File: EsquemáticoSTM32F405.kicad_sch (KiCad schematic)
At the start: 24 parts, among them SW3 XDTD-0304-215, U13 Green LED, U4 STM32F405RGT6, X1 32.768kHz 7pF SMD, X2 8Mhz 10pF

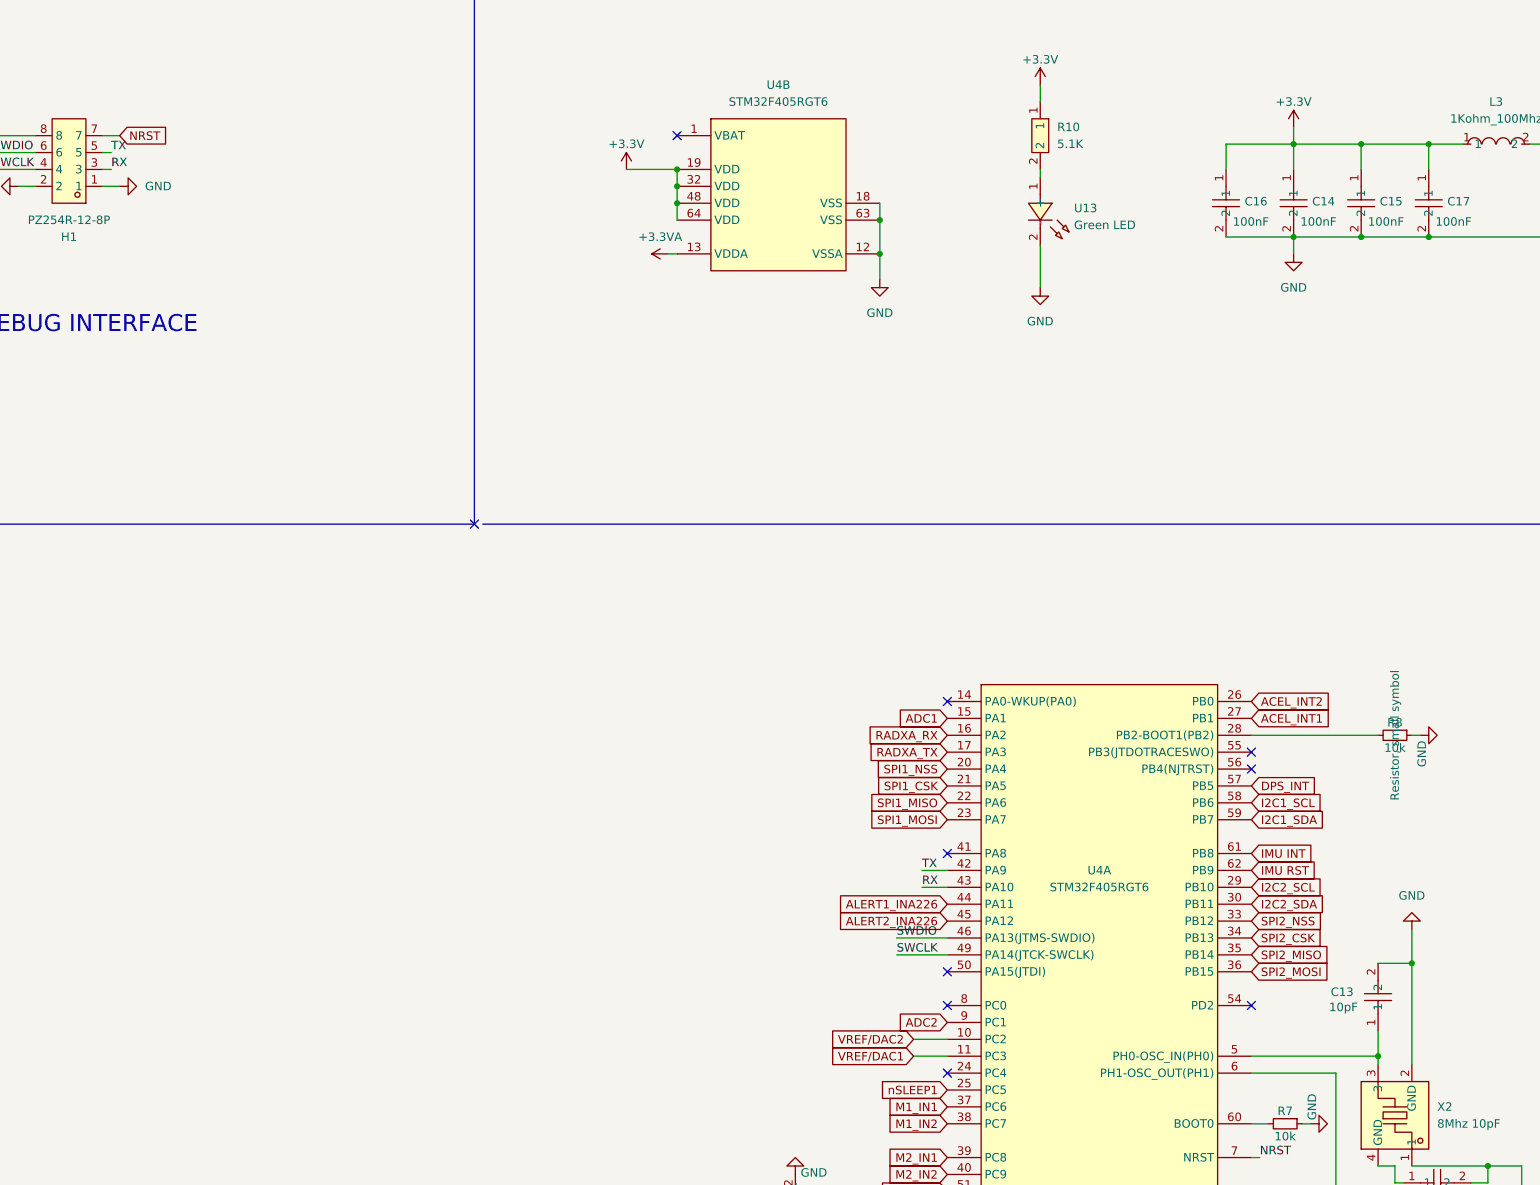
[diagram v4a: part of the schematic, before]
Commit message: Esquemático Versión mejorada
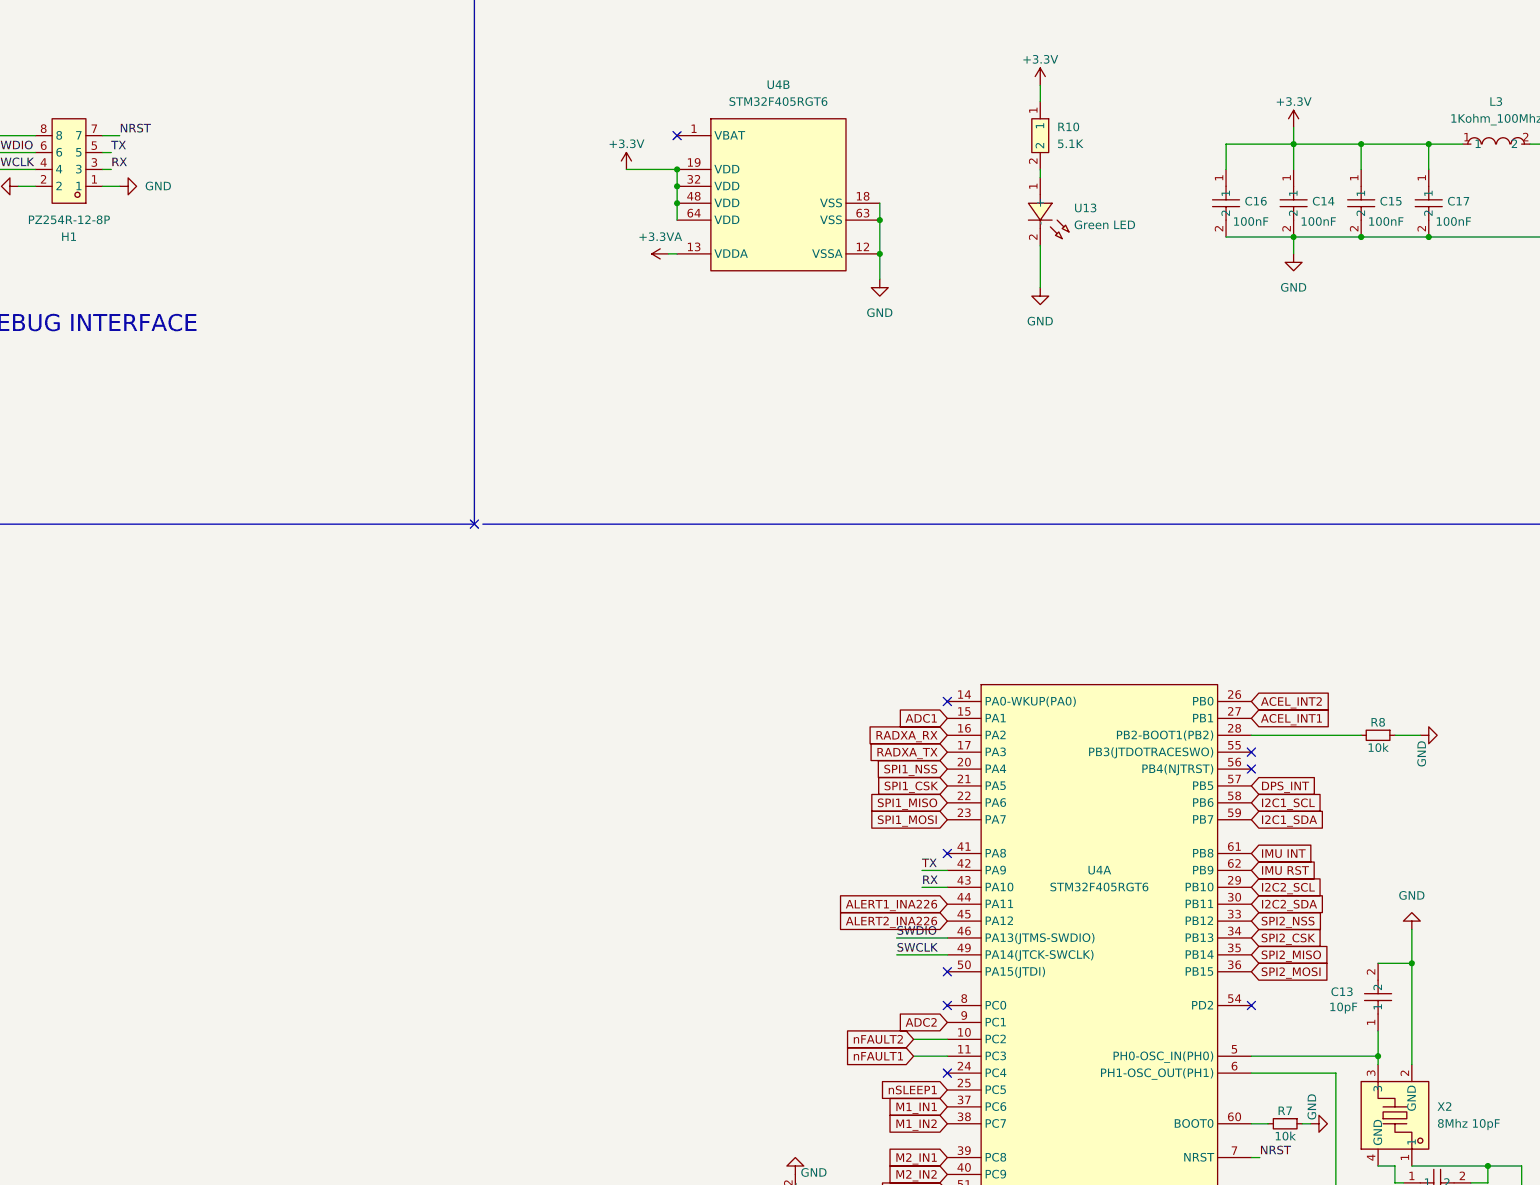
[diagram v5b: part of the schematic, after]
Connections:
- net VREF/DAC1 renamed nFAULT1
- net VREF/DAC2 renamed nFAULT2
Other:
- moved on the sheet: R8
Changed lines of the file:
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@@
 	(wire
 		(pts
-			(xy 358.14 138.43) (xy 359.41 138.43)
+			(xy 355.6 138.43) (xy 359.41 138.43)
 		)
 		(stroke
@@
 	(wire
 		(pts
-			(xy 334.01 138.43) (xy 353.06 138.43)
+			(xy 334.01 138.43) (xy 350.52 138.43)
 		)
 		(stroke
@@
 		)
 	)
+	(label "NRST"
+		(at 163.83 48.26 0)
+		(effects
+			(font
+				(size 1.27 1.27)
+			)
+			(justify left bottom)
+		)
+	)
 	(global_label "SPI2_MOSI"
 		(shape input)
@@
 		)
 	)
-	(global_label "VREF{slash}DAC2"
+	(global_label "nFAULT2"
 		(shape input)
 		(at 283.21 184.15 180)
@@
 		)
 		(property "Intersheetrefs" "${INTERSHEET_REFS}"
-			(at 269.46 184.15 0)
+			(at 272.3629 184.15 0)
 			(hide yes)
 			(show_name no)
@@
 		)
 	)
-	(global_label "VREF{slash}DAC1"
+	(global_label "nFAULT1"
 		(shape input)
 		(at 283.21 186.69 180)
@@
 		)
 		(property "Intersheetrefs" "${INTERSHEET_REFS}"
-			(at 269.46 186.69 0)
+			(at 272.3629 186.69 0)
 			(hide yes)
 			(show_name no)
@@
 		)
 	)
-	(global_label "NRST"
-		(shape input)
-		(at 163.83 48.26 0)
-		(effects
-			(font
-				(size 1.27 1.27)
-			)
-			(justify left)
-		)
-		(property "Intersheetrefs" "${INTERSHEET_REFS}"
-			(at 163.83 48.26 0)
-			(hide yes)
-			(show_name no)
-			(do_not_autoplace no)
-			(effects
-				(font
-					(size 1.27 1.27)
-				)
-			)
-		)
-	)
 	(global_label "I2C2_SCL"
 		(shape input)
@@
 	(symbol
 		(lib_id "Device:R_Small")
-		(at 355.6 138.43 270)
+		(at 353.06 138.43 270)
 		(unit 1)
 		(body_style 1)
@@
 		(dnp no)
 		(property "Reference" "R8"
-			(at 355.6 136.525 90)
+			(at 353.06 136.525 90)
 			(show_name no)
 			(do_not_autoplace no)
@@
 		)
 		(property "Value" "10k"
-			(at 355.6 140.335 90)
+			(at 353.06 140.335 90)
 			(show_name no)
 			(do_not_autoplace no)
@@
 		)
 		(property "Footprint" "Resistor_SMD:R_0402_1005Metric"
-			(at 355.6 138.43 0)
+			(at 353.06 138.43 0)
 			(hide yes)
 			(show_name no)
@@
 		)
 		(property "Datasheet" "~"
-			(at 355.6 138.43 0)
+			(at 353.06 138.43 0)
 			(hide yes)
 			(show_name no)
@@
 		)
 		(property "Description" "Resistor, small symbol"
-			(at 355.6 138.43 0)
+			(at 353.06 138.43 0)
+			(hide yes)
 			(show_name no)
 			(do_not_autoplace no)
@@
 		)
 		(property "LCSC Part #" "C25744"
-			(at 355.6 138.43 0)
+			(at 353.06 138.43 0)
 			(hide yes)
 			(show_name no)

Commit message: PCB ordenada V1
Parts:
- added R4, R5: 4.7K, ARLISS-footprints:R0603, symbol CANSAT_STM32_symbols:RC0603FR-074K7L
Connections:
- net +3.3V: now also R4.2, R5.2
- net DPS_INT: now also U4.24 (PC4); no longer U4.57 (PB5)
- net I2C1_SCL: now also R5.1
- net I2C1_SDA: now also R4.1
- net IMU INT: now also U4.2 (PC13); no longer U4.61 (PB8)
- net PIN_MOSFET: now also U4.61 (PB8); no longer U4.53 (PC12)
- net I2C2_SCL: no longer names the net of U4.29 (PB10)
- net I2C2_SDA: no longer names the net of U4.30 (PB11)
- no-connect marks 15 -> 17
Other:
- moved on the sheet: C11, C12, C13, C20, C21, C23, R7, R8, U4A, X1, X2

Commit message: Primer Ruteo de PCB
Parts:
- C11, C12, C13, C14, C15, C16, C17, C19, C22: footprint ARLISS-footprints:C0402 -> Capacitor_SMD:C_0402_1005Metric_Pad0.74x0.62mm_HandSolder
- C18: footprint Capacitor_SMD:C_0402_1005Metric -> Capacitor_SMD:C_0402_1005Metric_Pad0.74x0.62mm_HandSolder
- renumbered U13 to I1
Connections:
- net ADC1: now also U4.8 (PC0); no longer U4.15 (PA1)
- net GND: now also C12.1, X2.4 (GND)
- net OSC_IN: now reaches C12.2, X2.1
- net OSC_IN: now also U4.5 (PH0-OSC_IN(PH0)); no longer U4.6 (PH1-OSC_OUT(PH1))
- net ENCODER_B_1: now reaches U4.14 (PA0-WKUP(PA0))
- net OSC_OUT: now reaches C13.1, X2.3
- net OSC_OUT: now also U4.6 (PH1-OSC_OUT(PH1)); no longer U4.5 (PH0-OSC_IN(PH0))
- net ENCODER_A_1: now reaches U4.50 (PA15(JTDI))
- net ENCODER_A_2: now reaches U4.55 (PB3(JTDOTRACESWO))
- net RADXA_RX renamed RADXA_TX2
- net RADXA_TX renamed RADXA_RX2
- net RX renamed RX1
- net SPI1_CSK renamed SPI1_SCK
- net TX renamed TX1
- new net ENCODER_B_2: U4.15 (PA1)
- no-connect marks 17 -> 13
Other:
- moved on the sheet: C11, C12, C13, C20, C21, C23, R7, R8, U4A, X1, X2

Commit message: Arreglos de esquemático
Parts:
- removed I1: Green LED, ARLISS-footprints:LED0603-FD, symbol CANSAT_STM32_symbols:YLED0603G
- removed R10: 5.1K, Resistor_SMD:R_0402_1005Metric_Pad0.72x0.64mm_HandSolder, symbol CANSAT_STM32_symbols:FRC0402F5101TS
- removed SW3: XDTD-0304-215, ARLISS-footprints:SW-SMD_L3.9-W3.0-P4.45, symbol CANSAT_STM32_symbols:XDTD-0304-215
- added C26: 100nF, Capacitor_SMD:C_0402_1005Metric_Pad0.74x0.62mm_HandSolder, symbol CANSAT_STM32_symbols:TCC0402X7R104J500AT
- added LED3: D-R060306L3-KS2, Diode_SMD:D_0603_1608Metric_Pad1.05x0.95mm_HandSolder, symbol CANSAT_STM32_symbols:D-R060306L3-KS2
- added R10, R13: 1K, Resistor_SMD:R_0603_1608Metric_Pad0.98x0.95mm_HandSolder, symbol CANSAT_STM32_symbols:RC0603FR-071KL
- added R12: 10K, Resistor_SMD:R_0603_1608Metric_Pad0.98x0.95mm_HandSolder, symbol CANSAT_STM32_symbols:RC0603FR-7W10KL
- added SW3, SW4: EVQPLMA15, ARLISS-footprints:KEY-SMD_6P-L4.9-4.9-P3.70, symbol CANSAT_STM32_symbols:EVQPLMA15
- L3: footprint ARLISS-footprints:L0402 -> Inductor_SMD:L_0402_1005Metric_Pad0.77x0.64mm_HandSolder
- R11: value RC0603FR-7W10KL -> 10K; footprint ARLISS-footprints:R0603 -> Resistor_SMD:R_0603_1608Metric_Pad0.98x0.95mm_HandSolder
- R4, R5: footprint ARLISS-footprints:R0603 -> Resistor_SMD:R_0603_1608Metric_Pad0.98x0.95mm_HandSolder
- R7, R8: footprint Resistor_SMD:R_0402_1005Metric -> Resistor_SMD:R_0603_1608Metric_Pad0.98x0.95mm_HandSolder
- renumbered H1 to P1
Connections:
- net +3.3V: now also R12.2, R13.2
- net GND: now also C26.2, SW3.3, SW3.4, SW3.5 (GND), SW3.6 (GND), SW4.3, SW4.4, SW4.5 (GND), SW4.6 (GND)
- net NRST: now also SW4.1, SW4.2
- net FSM_button: now reaches U4.29 (PB10)
- net FSM_button: now also C26.1, R10.1
- net FSM_led: now reaches U4.30 (PB11)
- net FSM_led: now also LED3.1 (-)
- new net: R10.2, R12.1, SW3.1, SW3.2
- new net: LED3.2 (+), R13.1
- no-connect marks 13 -> 11
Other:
- note added: "FSM"
- moved on the sheet: C22, P1, R11
